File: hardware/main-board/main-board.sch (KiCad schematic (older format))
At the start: 38 parts, among them J2 STDC14, J3 NHD OLED Connector, U4 STM32F411RETx, U5 PAM8904EJP, U6 M24M01-RMN, Y1 16MHz

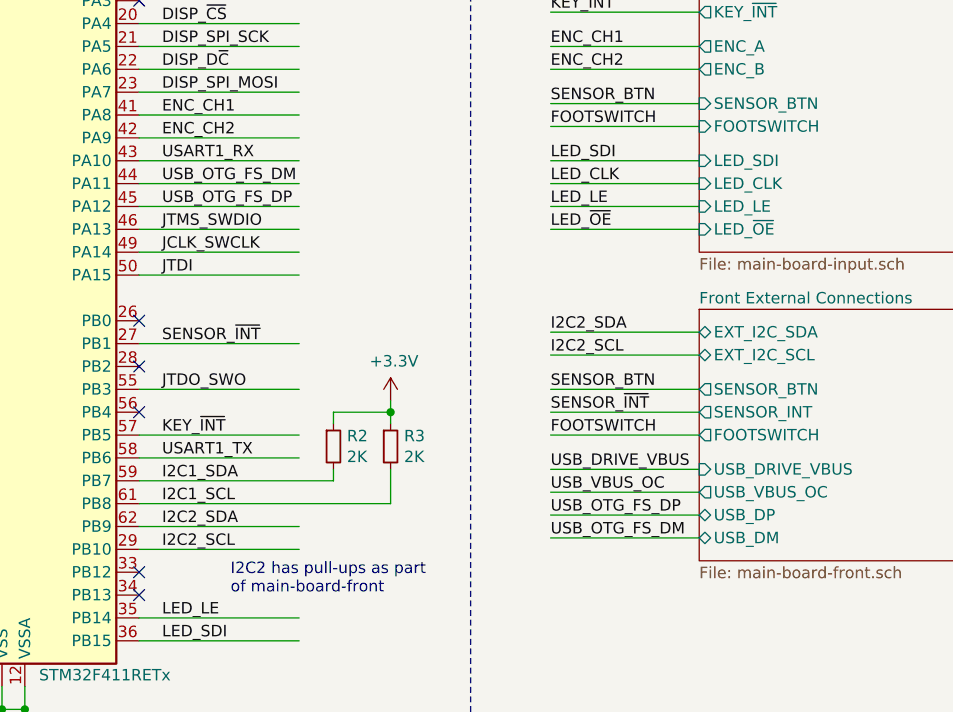
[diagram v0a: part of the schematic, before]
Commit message: Renamed USB nets so KiCad will recognize them correctly for routing
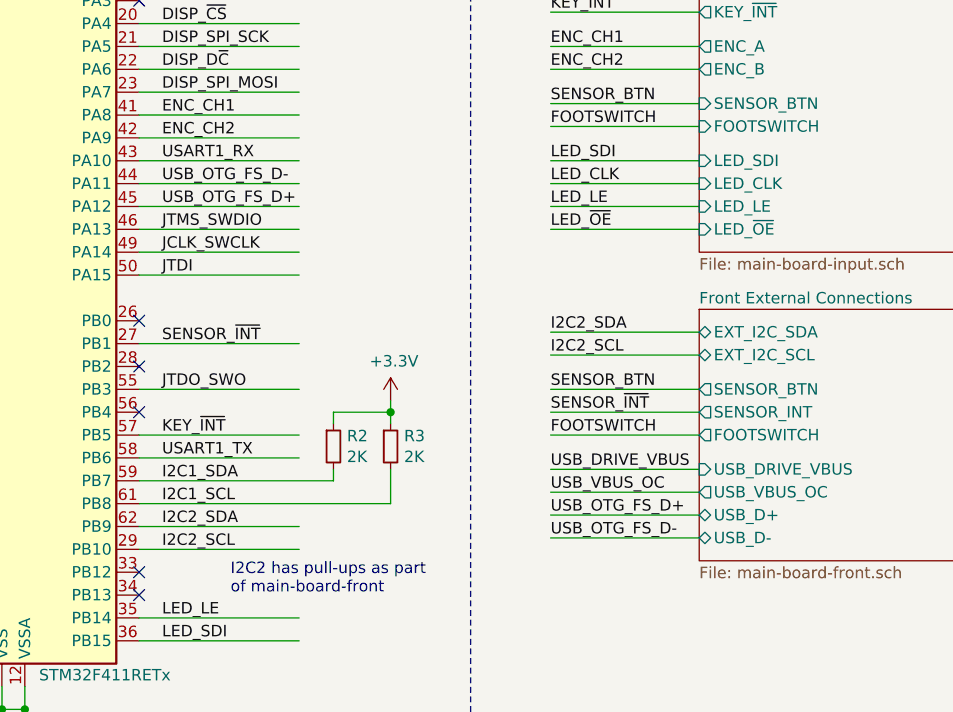
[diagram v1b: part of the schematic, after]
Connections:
- net labels added: USB_OTG_FS_D+, USB_OTG_FS_D-
- net labels removed: USB_OTG_FS_DM, USB_OTG_FS_DP
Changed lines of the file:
@@
 	4050 2700 4750 2700
 Text Label 4150 2800 0    50   ~ 0
-USB_OTG_FS_DM
+USB_OTG_FS_D-
 Text Label 4150 2900 0    50   ~ 0
-USB_OTG_FS_DP
+USB_OTG_FS_D+
 Wire Wire Line
 	4050 2800 4750 2800
@@
 SENSOR_~INT
 Text Label 5850 4350 0    50   ~ 0
-USB_OTG_FS_DM
+USB_OTG_FS_D-
 Text Label 5850 4250 0    50   ~ 0
-USB_OTG_FS_DP
+USB_OTG_FS_D+
 Text Label 5850 4050 0    50   ~ 0
 USB_DRIVE_VBUS
@@
 F7 "USB_DRIVE_VBUS" I L 6500 4050 50
 F8 "USB_VBUS_OC" O L 6500 4150 50
-F9 "USB_DP" B L 6500 4250 50
-F10 "USB_DM" B L 6500 4350 50
+F9 "USB_D+" B L 6500 4250 50
+F10 "USB_D-" B L 6500 4350 50
 $EndSheet
 Text Label 5850 2200 0    50   ~ 0

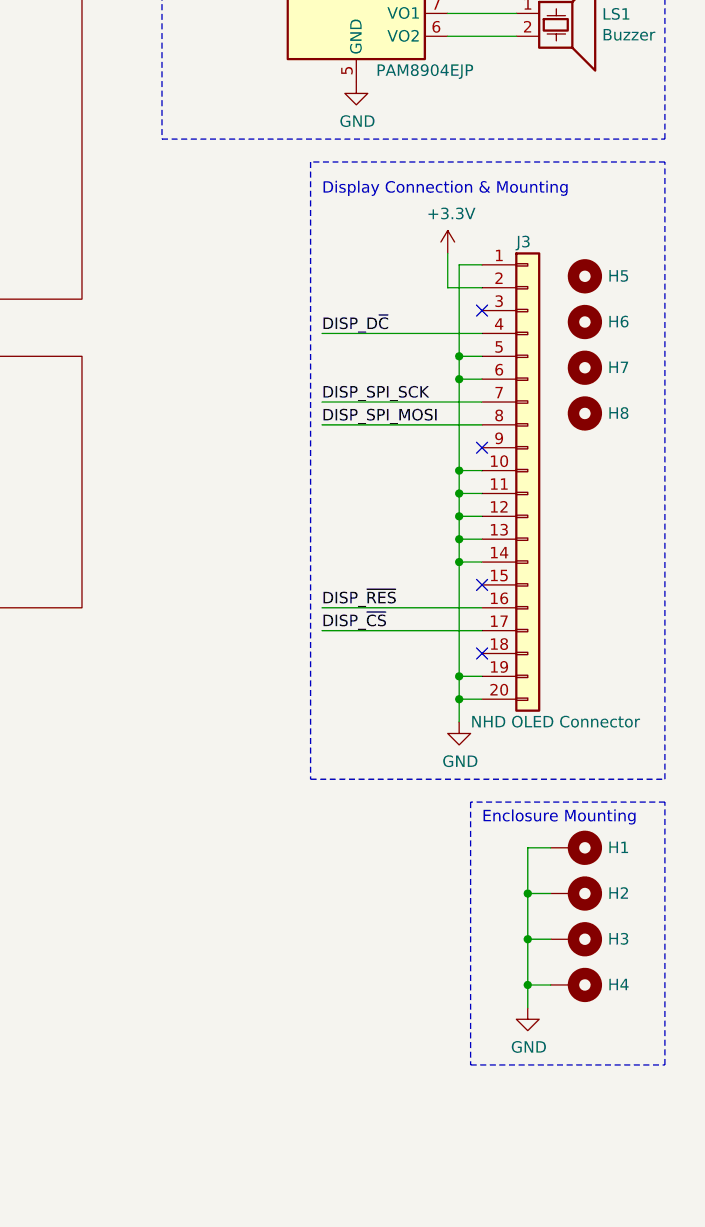
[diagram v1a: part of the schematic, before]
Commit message: Implemented a dedicated symbol/footprint for the NHD-3.12 display
The footprint combines the pin socket/header connector with correctly
aligned mounting holes, to make PCB layout easier.

The symbol labels the pins for the display module's serial interface, to
make the schematic a little bit nicer.

Included the STEP model of the display from the NHD website.

Functionally, its not that different than before.
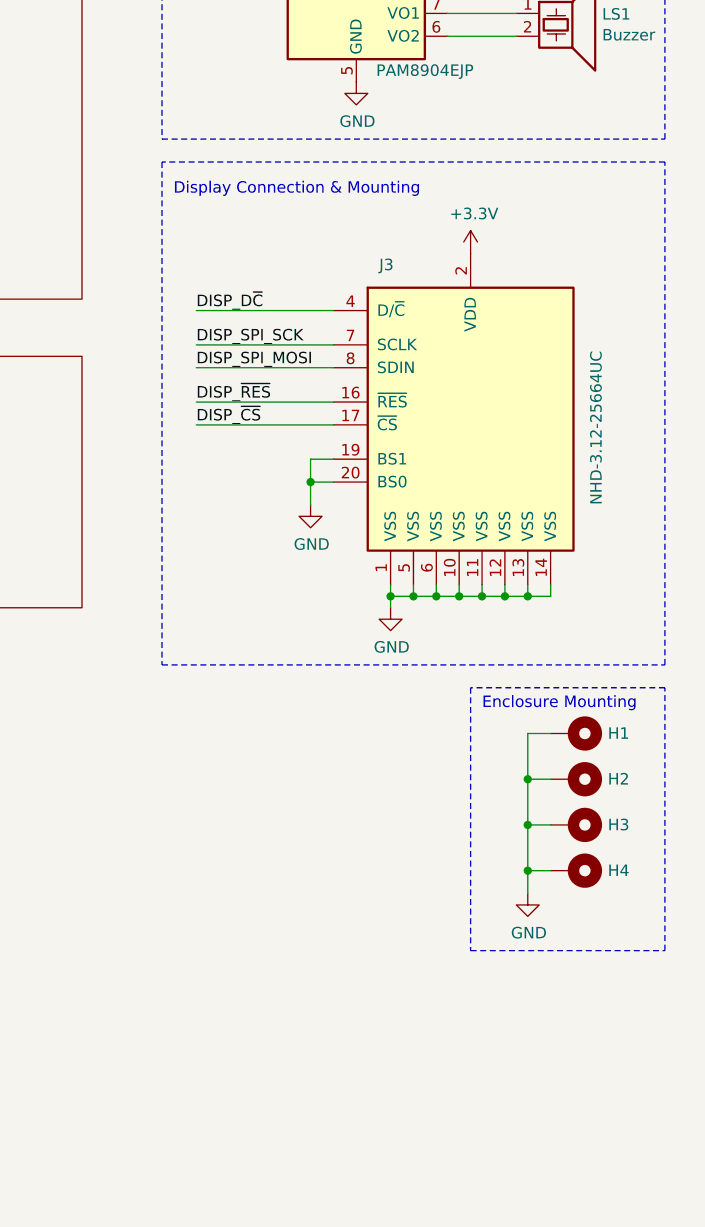
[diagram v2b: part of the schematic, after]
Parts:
- removed H5, H6, H7, H8: MountingHole, MountingHole:MountingHole_2.7mm_M2.5_Pad, symbol Mechanical:MountingHole
- removed J3: NHD OLED Connector, Connector_PinSocket_2.54mm:PinSocket_1x20_P2.54mm_Vertical, symbol Connector_Generic:Conn_01x20
- added J3: NHD-3.12-25664UC, lib_fp:NHD-3.12-25664, symbol Project:NHD-3.12-25664UC
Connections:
- wire segments 214 -> 212
- no-connect marks 26 -> 22
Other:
- moved on the sheet: H1, H2, H3, H4

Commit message: Fix BOM assignments for PAM8904E
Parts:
- U5: Description AUDIO HIGH VOLT U-QFN3030-16 -> AUDIO HIGH VOLT U-QFN3030-12; Manufacturer PN PAM8904EJER -> PAM8904EJPR; Supplier PN 31-PAM8904EJERCT-ND -> 31-PAM8904EJPRCT-ND
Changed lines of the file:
@@
 F 2 "lib_fp:U-QFN3030-12_Type-A" H 9100 550 50  0001 C CNN
 F 3 "https://www.diodes.com/assets/Datasheets/PAM8904E.pdf" H 9100 1550 50  0001 C CNN
-F 4 "AUDIO HIGH VOLT U-QFN3030-16" H 9100 1550 50  0001 C CNN "Description"
+F 4 "AUDIO HIGH VOLT U-QFN3030-12" H 9100 1550 50  0001 C CNN "Description"
 F 5 "Diodes Incorporated" H 9100 1550 50  0001 C CNN "Manufacturer"
-F 6 "PAM8904EJER" H 9100 1550 50  0001 C CNN "Manufacturer PN"
+F 6 "PAM8904EJPR" H 9100 1550 50  0001 C CNN "Manufacturer PN"
 F 7 "Digi-Key" H 9100 1550 50  0001 C CNN "Supplier"
-F 8 "31-PAM8904EJERCT-ND" H 9100 1550 50  0001 C CNN "Supplier PN"
+F 8 "31-PAM8904EJPRCT-ND" H 9100 1550 50  0001 C CNN "Supplier PN"
 	1    9100 1550
 	1    0    0    -1

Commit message: Schematic cleanup
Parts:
- U4: value STM32F411RETx -> STM32F411RET6
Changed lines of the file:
@@
 P 3350 3200
 F 0 "U4" H 2800 4850 50  0000 C CNN
-F 1 "STM32F411RETx" H 3900 1450 50  0000 C CNN
+F 1 "STM32F411RET6" H 3900 1450 50  0000 C CNN
 F 2 "Package_QFP:LQFP-64_10x10mm_P0.5mm" H 2750 1500 50  0001 R CNN
 F 3 "http://www.st.com/st-web-ui/static/active/en/resource/technical/document/datasheet/DM00115249.pdf" H 3350 3200 50  0001 C CNN
@@
 $EndComp
 $Sheet
-S 6500 750  1400 750
+S 6500 800  1400 750
 U 5F8B674D
 F0 "Power Supply and Control" 50
 F1 "main-board-power.sch" 50
-F2 "RELAY_ENLARGER" I L 6500 850 50
-F3 "RELAY_SAFELIGHT" I L 6500 950 50
+F2 "RELAY_ENLARGER" I L 6500 900 50
+F3 "RELAY_SAFELIGHT" I L 6500 1000 50
 $EndSheet
 $Sheet
-S 6500 1750 1400 1350
+S 6500 1800 1400 1350
 U 5F8B69B5
 F0 "User Input" 50
 F1 "main-board-input.sch" 50
-F2 "INT_I2C_SDA" B L 6500 1850 50
-F3 "INT_I2C_SCL" B L 6500 1950 50
-F4 "SENSOR_BTN" I L 6500 2450 50
-F5 "FOOTSWITCH" I L 6500 2550 50
-F6 "LED_SDI" I L 6500 2700 50
-F7 "LED_CLK" I L 6500 2800 50
-F8 "LED_LE" I L 6500 2900 50
-F9 "LED_~OE" I L 6500 3000 50
-F10 "KEY_~INT" O L 6500 2050 50
-F11 "ENC_A" O L 6500 2200 50
-F12 "ENC_B" O L 6500 2300 50
+F2 "INT_I2C_SDA" B L 6500 1900 50
+F3 "INT_I2C_SCL" B L 6500 2000 50
+F4 "SENSOR_BTN" I L 6500 2500 50
+F5 "FOOTSWITCH" I L 6500 2600 50
+F6 "LED_SDI" I L 6500 2750 50
+F7 "LED_CLK" I L 6500 2850 50
+F8 "LED_LE" I L 6500 2950 50
+F9 "LED_~OE" I L 6500 3050 50
+F10 "KEY_~INT" O L 6500 2100 50
+F11 "ENC_A" O L 6500 2250 50
+F12 "ENC_B" O L 6500 2350 50
 $EndSheet
 $Comp
@@
 Can swap connections on ESD\nprotection to optimize routing
 NoConn ~ 1350 5700
-Text Label 5850 3550 0    50   ~ 0
+Text Label 5850 3600 0    50   ~ 0
 I2C2_SCL
-Text Label 5850 3450 0    50   ~ 0
+Text Label 5850 3500 0    50   ~ 0
 I2C2_SDA
-Text Label 5850 3800 0    50   ~ 0
+Text Label 5850 3850 0    50   ~ 0
 SENSOR_~INT
-Text Label 5850 4350 0    50   ~ 0
+Text Label 5850 4400 0    50   ~ 0
 USB_OTG_FS_D-
-Text Label 5850 4250 0    50   ~ 0
+Text Label 5850 4300 0    50   ~ 0
 USB_OTG_FS_D+
-Text Label 5850 4050 0    50   ~ 0
+Text Label 5850 4100 0    50   ~ 0
 USB_DRIVE_VBUS
-Text Label 5850 4150 0    50   ~ 0
+Text Label 5850 4200 0    50   ~ 0
 USB_VBUS_OC
-Text Label 5850 2450 0    50   ~ 0
+Text Label 5850 2500 0    50   ~ 0
 SENSOR_BTN
-Text Label 5850 2550 0    50   ~ 0
+Text Label 5850 2600 0    50   ~ 0
 FOOTSWITCH
-Text Label 5850 3700 0    50   ~ 0
+Text Label 5850 3750 0    50   ~ 0
 SENSOR_BTN
-Text Label 5850 3900 0    50   ~ 0
+Text Label 5850 3950 0    50   ~ 0
 FOOTSWITCH
 Wire Wire Line
-	6500 2450 5850 2450
-Wire Wire Line
-	5850 2550 6500 2550
-Text Label 5850 1850 0    50   ~ 0
+	6500 2500 5850 2500
+Wire Wire Line
+	5850 2600 6500 2600
+Text Label 5850 1900 0    50   ~ 0
 I2C1_SDA
-Text Label 5850 1950 0    50   ~ 0
+Text Label 5850 2000 0    50   ~ 0
 I2C1_SCL
 Wire Wire Line
-	5850 1950 6500 1950
-Wire Wire Line
-	5850 1850 6500 1850
-Text Label 5850 2050 0    50   ~ 0
+	5850 2000 6500 2000
+Wire Wire Line
+	5850 1900 6500 1900
+Text Label 5850 2100 0    50   ~ 0
 KEY_~INT
 Wire Wire Line
-	5850 2050 6500 2050
-Text Notes 4450 4600 0    50   ~ 0
+	5850 2100 6500 2100
+Text Notes 4150 4600 0    50   ~ 0
 I2C2 has pull-ups as part\nof main-board-front
-Text Label 5850 950  0    50   ~ 0
+Text Label 5850 1000 0    50   ~ 0
 RELAY_SFLT
-Text Label 5850 850  0    50   ~ 0
+Text Label 5850 900  0    50   ~ 0
 RELAY_ENLG
 Wire Wire Line
-	6500 850  5850 850
-Wire Wire Line
-	6500 950  5850 950
+	6500 900  5850 900
+Wire Wire Line
+	6500 1000 5850 1000
 Text Label 2000 4100 0    50   ~ 0
 RELAY_SFLT
@@
 U 1 1 5FA699B6
 P 4000 5900
-F 0 "C23" V 4150 5750 50  0000 L CNN
+F 0 "C23" V 4125 5725 50  0000 L CNN
 F 1 "0.1uF" V 4050 5650 50  0000 L CNN
 F 2 "Capacitor_SMD:C_0603_1608Metric" H 4000 5900 50  0001 C CNN
@@
 Wire Wire Line
 	4050 4800 4750 4800
-Text Label 5850 3000 0    50   ~ 0
+Text Label 5850 3050 0    50   ~ 0
 LED_~OE
-Text Label 5850 2800 0    50   ~ 0
+Text Label 5850 2850 0    50   ~ 0
 LED_CLK
-Text Label 5850 2900 0    50   ~ 0
+Text Label 5850 2950 0    50   ~ 0
 LED_LE
-Text Label 5850 2700 0    50   ~ 0
+Text Label 5850 2750 0    50   ~ 0
 LED_SDI
 Wire Wire Line
-	6500 2700 5850 2700
-Wire Wire Line
-	6500 2800 5850 2800
-Wire Wire Line
-	6500 2900 5850 2900
-Wire Wire Line
-	6500 3000 5850 3000
+	6500 2750 5850 2750
+Wire Wire Line
+	6500 2850 5850 2850
+Wire Wire Line
+	6500 2950 5850 2950
+Wire Wire Line
+	6500 3050 5850 3050
 NoConn ~ 4050 2000
 NoConn ~ 4050 3400
@@
 NoConn ~ 1100 7100
 Wire Wire Line
-	5850 4350 6500 4350
-Wire Wire Line
-	5850 4250 6500 4250
-Wire Wire Line
-	5850 4150 6500 4150
-Wire Wire Line
-	6500 4050 5850 4050
-Wire Wire Line
-	5850 3900 6500 3900
-Wire Wire Line
-	5850 3800 6500 3800
-Wire Wire Line
-	5850 3700 6500 3700
-Wire Wire Line
-	5850 3550 6500 3550
-Wire Wire Line
-	6500 3450 5850 3450
+	5850 4400 6500 4400
+Wire Wire Line
+	5850 4300 6500 4300
+Wire Wire Line
+	5850 4200 6500 4200
+Wire Wire Line
+	6500 4100 5850 4100
+Wire Wire Line
+	5850 3950 6500 3950
+Wire Wire Line
+	5850 3850 6500 3850
+Wire Wire Line
+	5850 3750 6500 3750
+Wire Wire Line
+	5850 3600 6500 3600
+Wire Wire Line
+	6500 3500 5850 3500
 $Sheet
-S 6500 3350 1400 1100
+S 6500 3400 1400 1100
 U 5FA19AFF
 F0 "Front External Connections" 50
 F1 "main-board-front.sch" 50
-F2 "EXT_I2C_SDA" B L 6500 3450 50
-F3 "EXT_I2C_SCL" B L 6500 3550 50
-F4 "SENSOR_BTN" O L 6500 3700 50
-F5 "SENSOR_INT" O L 6500 3800 50
-F6 "FOOTSWITCH" O L 6500 3900 50
-F7 "USB_DRIVE_VBUS" I L 6500 4050 50
-F8 "USB_VBUS_OC" O L 6500 4150 50
-F9 "USB_D+" B L 6500 4250 50
-F10 "USB_D-" B L 6500 4350 50
+F2 "EXT_I2C_SDA" B L 6500 3500 50
+F3 "EXT_I2C_SCL" B L 6500 3600 50
+F4 "SENSOR_BTN" O L 6500 3750 50
+F5 "SENSOR_INT" O L 6500 3850 50
+F6 "FOOTSWITCH" O L 6500 3950 50
+F7 "USB_DRIVE_VBUS" I L 6500 4100 50
+F8 "USB_VBUS_OC" O L 6500 4200 50
+F9 "USB_D+" B L 6500 4300 50
+F10 "USB_D-" B L 6500 4400 50
 $EndSheet
-Text Label 5850 2200 0    50   ~ 0
+Text Label 5850 2250 0    50   ~ 0
 ENC_CH1
-Text Label 5850 2300 0    50   ~ 0
+Text Label 5850 2350 0    50   ~ 0
 ENC_CH2
 Wire Wire Line
-	5850 2200 6500 2200
-Wire Wire Line
-	5850 2300 6500 2300
+	5850 2250 6500 2250
+Wire Wire Line
+	5850 2350 6500 2350
 Text Label 4150 1800 0    50   ~ 0
 BUZZ_EN2
@@
 Wire Notes Line
 	10450 2500 8250 2500
+Wire Notes Line
+	5600 550  8150 550
+Wire Notes Line
+	8150 550  8150 4700
+Wire Notes Line
+	8150 4700 5600 4700
+Wire Notes Line
+	5600 4700 5600 550
 $EndSCHEMATC

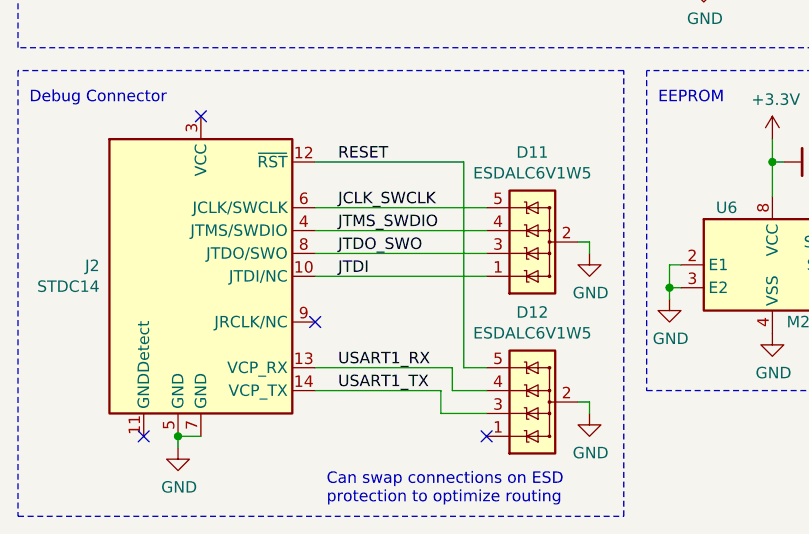
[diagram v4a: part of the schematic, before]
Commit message: First pass at doing PCB layout, all nets connected and DRC passes
Setup design rules based on a JLCPCB 4-layer board, taking initial
defaults from a combination of previous settings and various
example/template projects.

Placed all panel-mount components in dimensionally accurate locations,
and locked their footprints. These locations are based on their
datasheets and mockups of the device case panels.

Placed, arranged, and routed all PCB components. This is a first pass at
routing, so there is definitely room for tweaking and improvement.
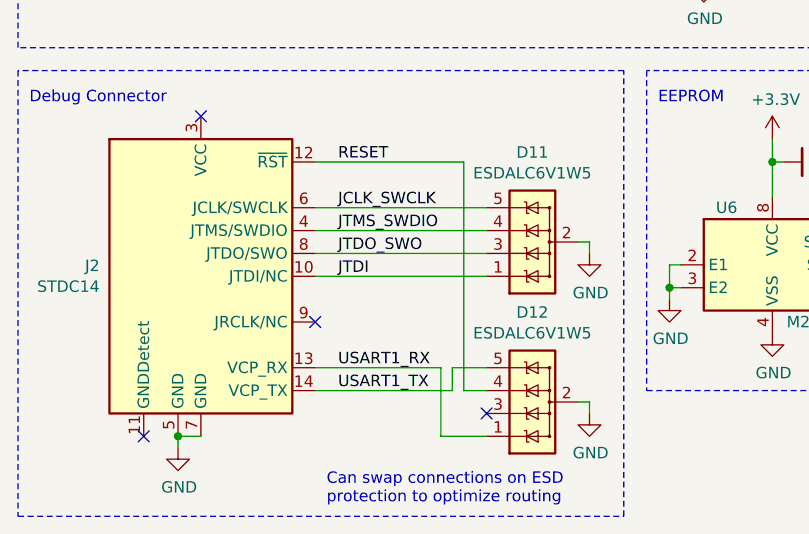
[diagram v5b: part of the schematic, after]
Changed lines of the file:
@@
 	1850 6400 2600 6400
 Wire Wire Line
-	1850 6800 2450 6800
-Wire Wire Line
-	1850 6900 2400 6900
-NoConn ~ 2600 7100
+	1850 6800 2400 6800
+Wire Wire Line
+	1850 6900 2450 6900
+NoConn ~ 2600 7000
 $Comp
 L power:GND #PWR012
@@
 USART1_TX
 Wire Wire Line
-	2400 6900 2400 7000
-Wire Wire Line
-	2400 7000 2600 7000
-Wire Wire Line
-	2450 6800 2450 6900
-Wire Wire Line
-	2450 6900 2600 6900
-Wire Wire Line
-	2500 5900 2500 6800
-Wire Wire Line
-	2500 6800 2600 6800
+	2500 5900 2500 6900
 Text Notes 1900 7400 0    50   ~ 0
 Can swap connections on ESD\nprotection to optimize routing
@@
 Wire Notes Line
 	5600 4700 5600 550
+Wire Wire Line
+	2500 6900 2600 6900
+Wire Wire Line
+	2450 6900 2450 6800
+Wire Wire Line
+	2450 6800 2600 6800
+Wire Wire Line
+	2400 6800 2400 7100
+Wire Wire Line
+	2400 7100 2600 7100
 $EndSCHEMATC

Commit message: PCB layout cleanup and minor fixes
Tweaked traces all over the PCB
Increased size of capacitor on USB VBUS
Added ground connections to the crystal case
Slightly increased the size of the isolated ground around the crystal
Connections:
- wire segments 212 -> 218
- no-connect marks 22 -> 20
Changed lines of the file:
@@
 U 1 1 5F94F8E6
 P 1200 3150
-F 0 "Y1" H 1250 3350 50  0000 L CNN
-F 1 "16MHz" H 1225 2950 50  0000 L CNN
+F 0 "Y1" H 1200 3550 50  0000 C CNN
+F 1 "16MHz" H 1200 3450 50  0000 C CNN
 F 2 "lib_fp:Crystal_SMD_Kyocera_CX3225GB" H 1200 3150 50  0001 C CNN
 F 3 "http://prdct-search.kyocera.co.jp/crystal-ic/catalog/en/cx3225gb_e.pdf" H 1200 3150 50  0001 C CNN
@@
 	1    0    0    -1
 $EndComp
-NoConn ~ 1200 3350
-NoConn ~ 1200 2950
 $Comp
 L Project:M24M01-RMN U6
@@
 Wire Wire Line
 	2400 7100 2600 7100
+$Comp
+L power:GND #PWR?
+U 1 1 5FAE5C8E
+P 1200 3450
+F 0 "#PWR?" H 1200 3200 50  0001 C CNN
+F 1 "GND" H 1205 3277 50  0000 C CNN
+F 2 "" H 1200 3450 50  0001 C CNN
+F 3 "" H 1200 3450 50  0001 C CNN
+	1    1200 3450
+	1    0    0    -1
+$EndComp
+Wire Wire Line
+	1200 2950 1200 2900
+Wire Wire Line
+	1200 2900 1400 2900
+Wire Wire Line
+	1400 2900 1400 3400
+Wire Wire Line
+	1400 3400 1200 3400
+Wire Wire Line
+	1200 3350 1200 3400
+Connection ~ 1200 3400
+Wire Wire Line
+	1200 3400 1200 3450
 $EndSCHEMATC
